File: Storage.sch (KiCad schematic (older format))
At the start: 22 parts, among them J8 Micro_SD_Card_Det, U17 FTDITypeUART, U18 ABRACON-ASDMB, U19 S25FL256SAGNFI001, U20 xc7z020clg484

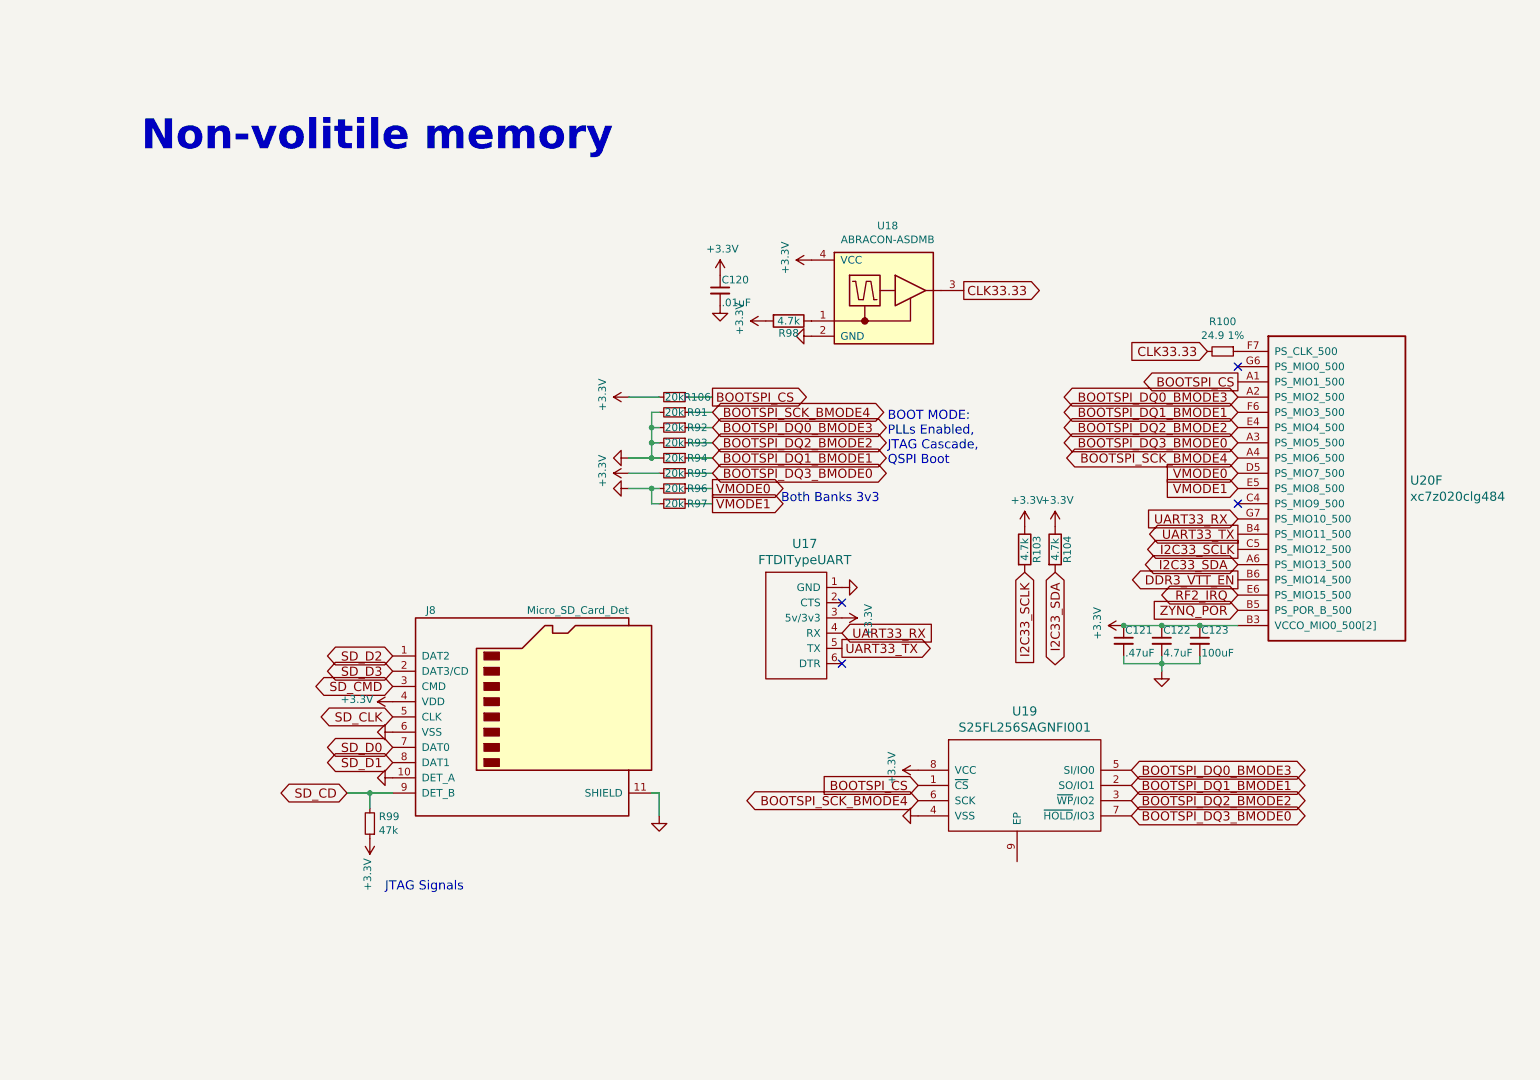
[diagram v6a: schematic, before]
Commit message: somehow the zones got messed up. fixing them
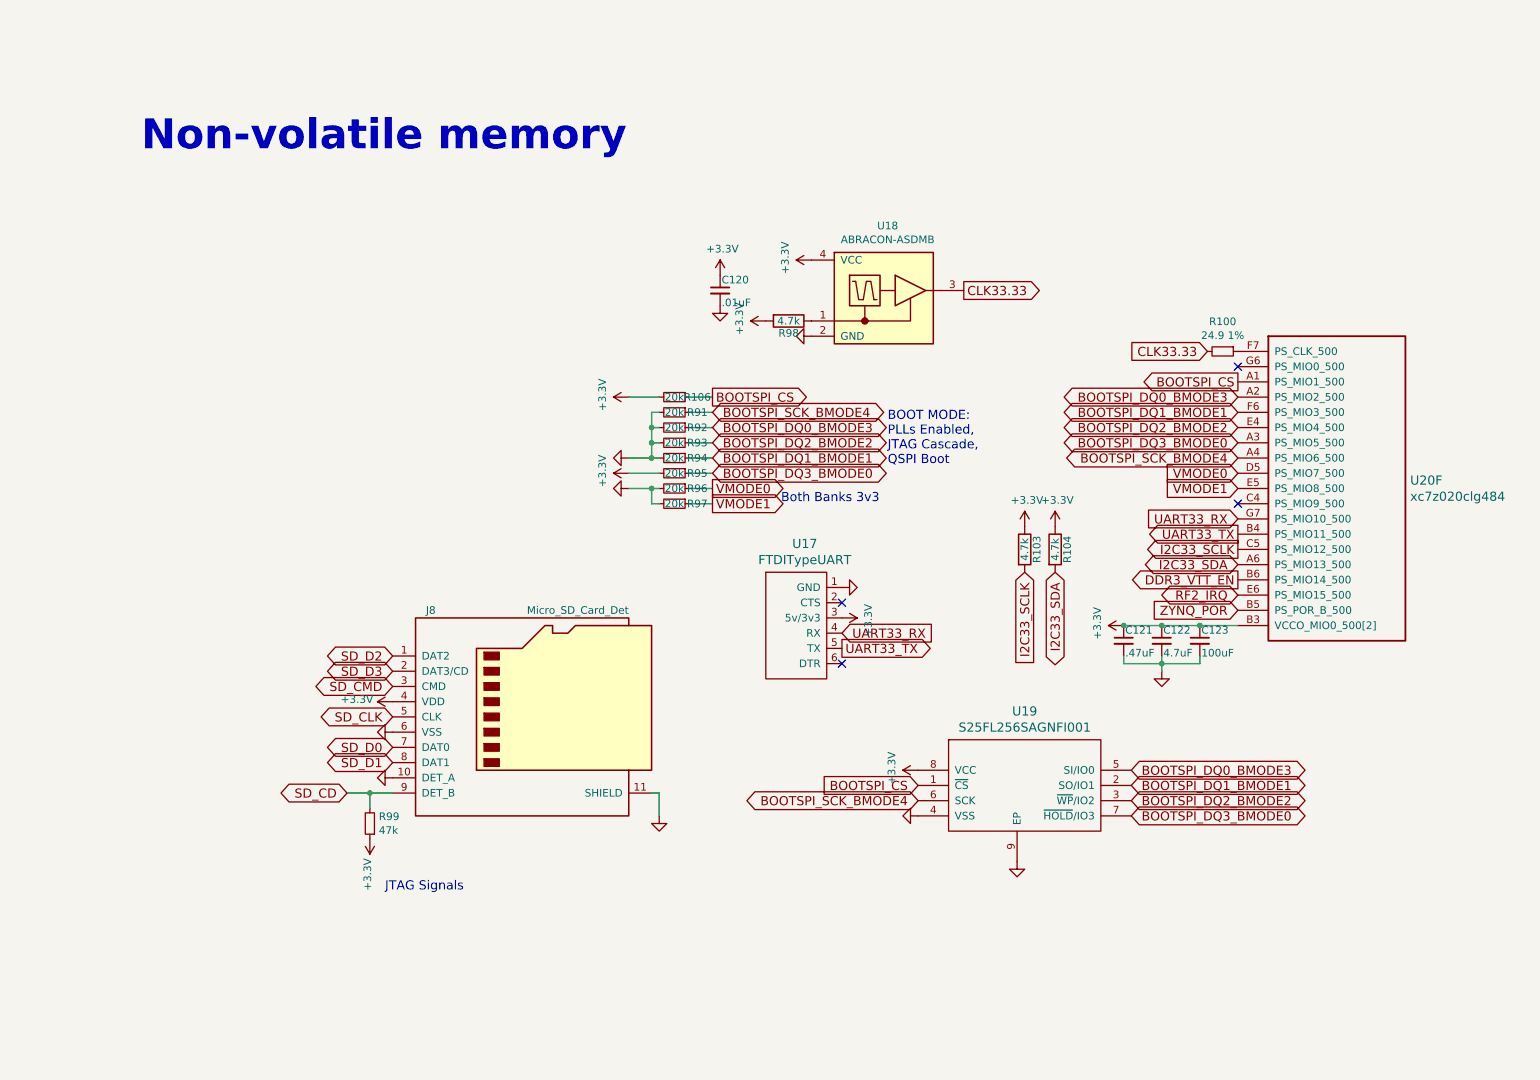
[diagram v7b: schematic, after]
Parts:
- U19: footprint DFTcustom:WSON-8 -> footprints:Cypress-002-18827-0-0-0
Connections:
- net GND: now also U19.9 (EP)
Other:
- note added: "Non-volatile memory"
- note removed: "Non-volitile memory"
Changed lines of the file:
@@
 EESchema Schematic File Version 4
-EELAYER 30 0
+LIBS:DFTBoard-cache
+EELAYER 26 0
 EELAYER END
 $Descr A4 11693 8268
@@
 F 0 "U19" H 6750 5787 60  0000 C CNN
 F 1 "S25FL256SAGNFI001" H 6750 5681 60  0000 C CNN
-F 2 "DFTcustom:WSON-8" H 6350 6300 60  0001 C CNN
+F 2 "footprints:Cypress-002-18827-0-0-0" H 6350 6300 60  0001 C CNN
 F 3 "" H 6350 6300 60  0001 C CNN
 F 4 "Cypress" H 0   0   50  0001 C CNN "MFR"
@@
 I2C33_SDA
 Text Notes 950  1150 0    197  ~ 39
-Non-volitile memory
+Non-volatile memory
 Text GLabel 6750 3900 3    60   Input ~ 0
 I2C33_SCLK
@@
 NoConn ~ 8150 2550
 NoConn ~ 8150 3450
+$Comp
+L power:GND #PWR?
+U 1 1 6034A13B
+P 6700 5800
+AR Path="/58508414/6034A13B" Ref="#PWR?"  Part="1"
+AR Path="/5852A88E/6034A13B" Ref="#PWR?"  Part="1"
+AR Path="/5CA1ABAE/6034A13B" Ref="#PWR0357"  Part="1"
+F 0 "#PWR0357" H 6700 5800 30  0001 C CNN
+F 1 "GND" H 6700 5730 30  0001 C CNN
+F 2 "" H 6700 5800 60  0001 C CNN
+F 3 "" H 6700 5800 60  0001 C CNN
+	1    6700 5800
+	1    0    0    -1
+$EndComp
 $EndSCHEMATC
